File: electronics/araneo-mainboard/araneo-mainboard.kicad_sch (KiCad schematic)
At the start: 57 parts, among them J1 GPIO, J2 OLED, SW1 SW, U1 IMU, U2 L78M05CDT, U3 BD9C601EFJ, U4 POWER, U5 PAM8403D

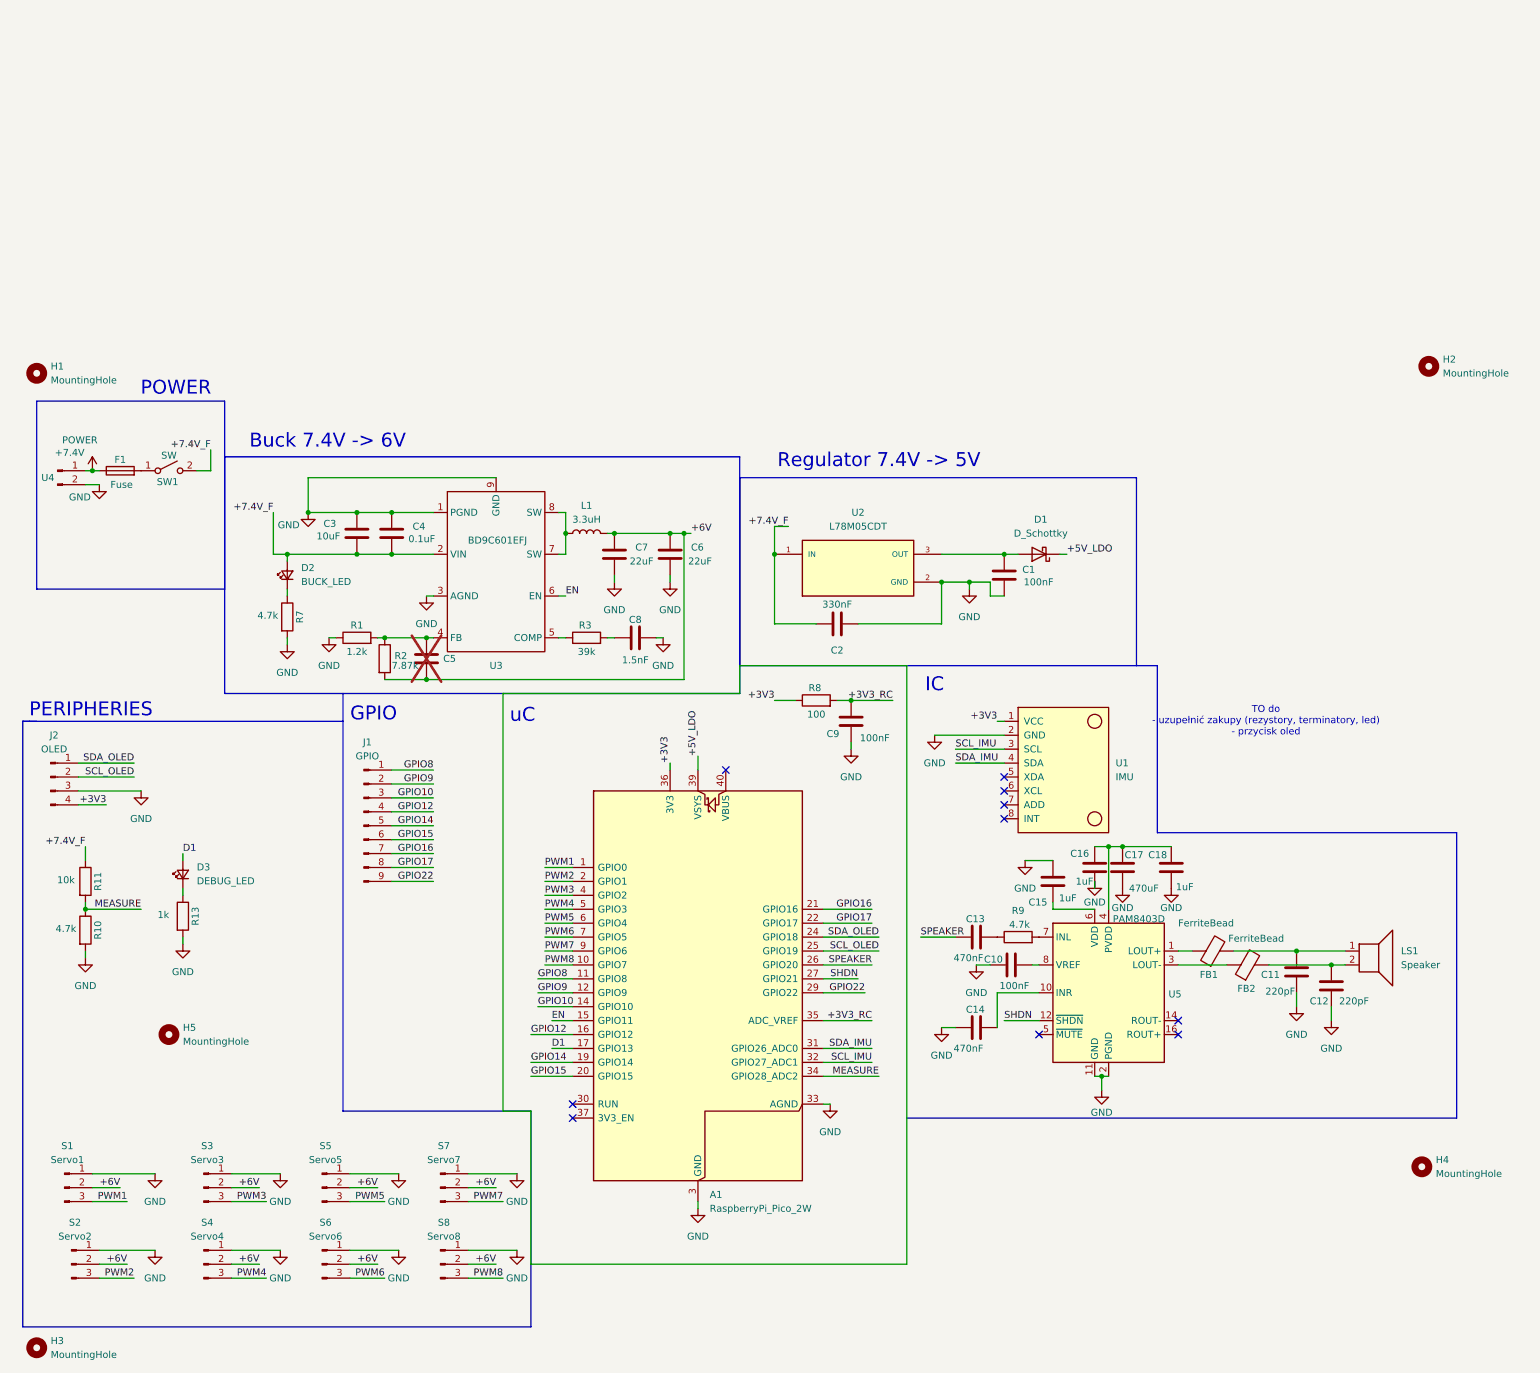
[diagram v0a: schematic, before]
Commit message: electronics: add button
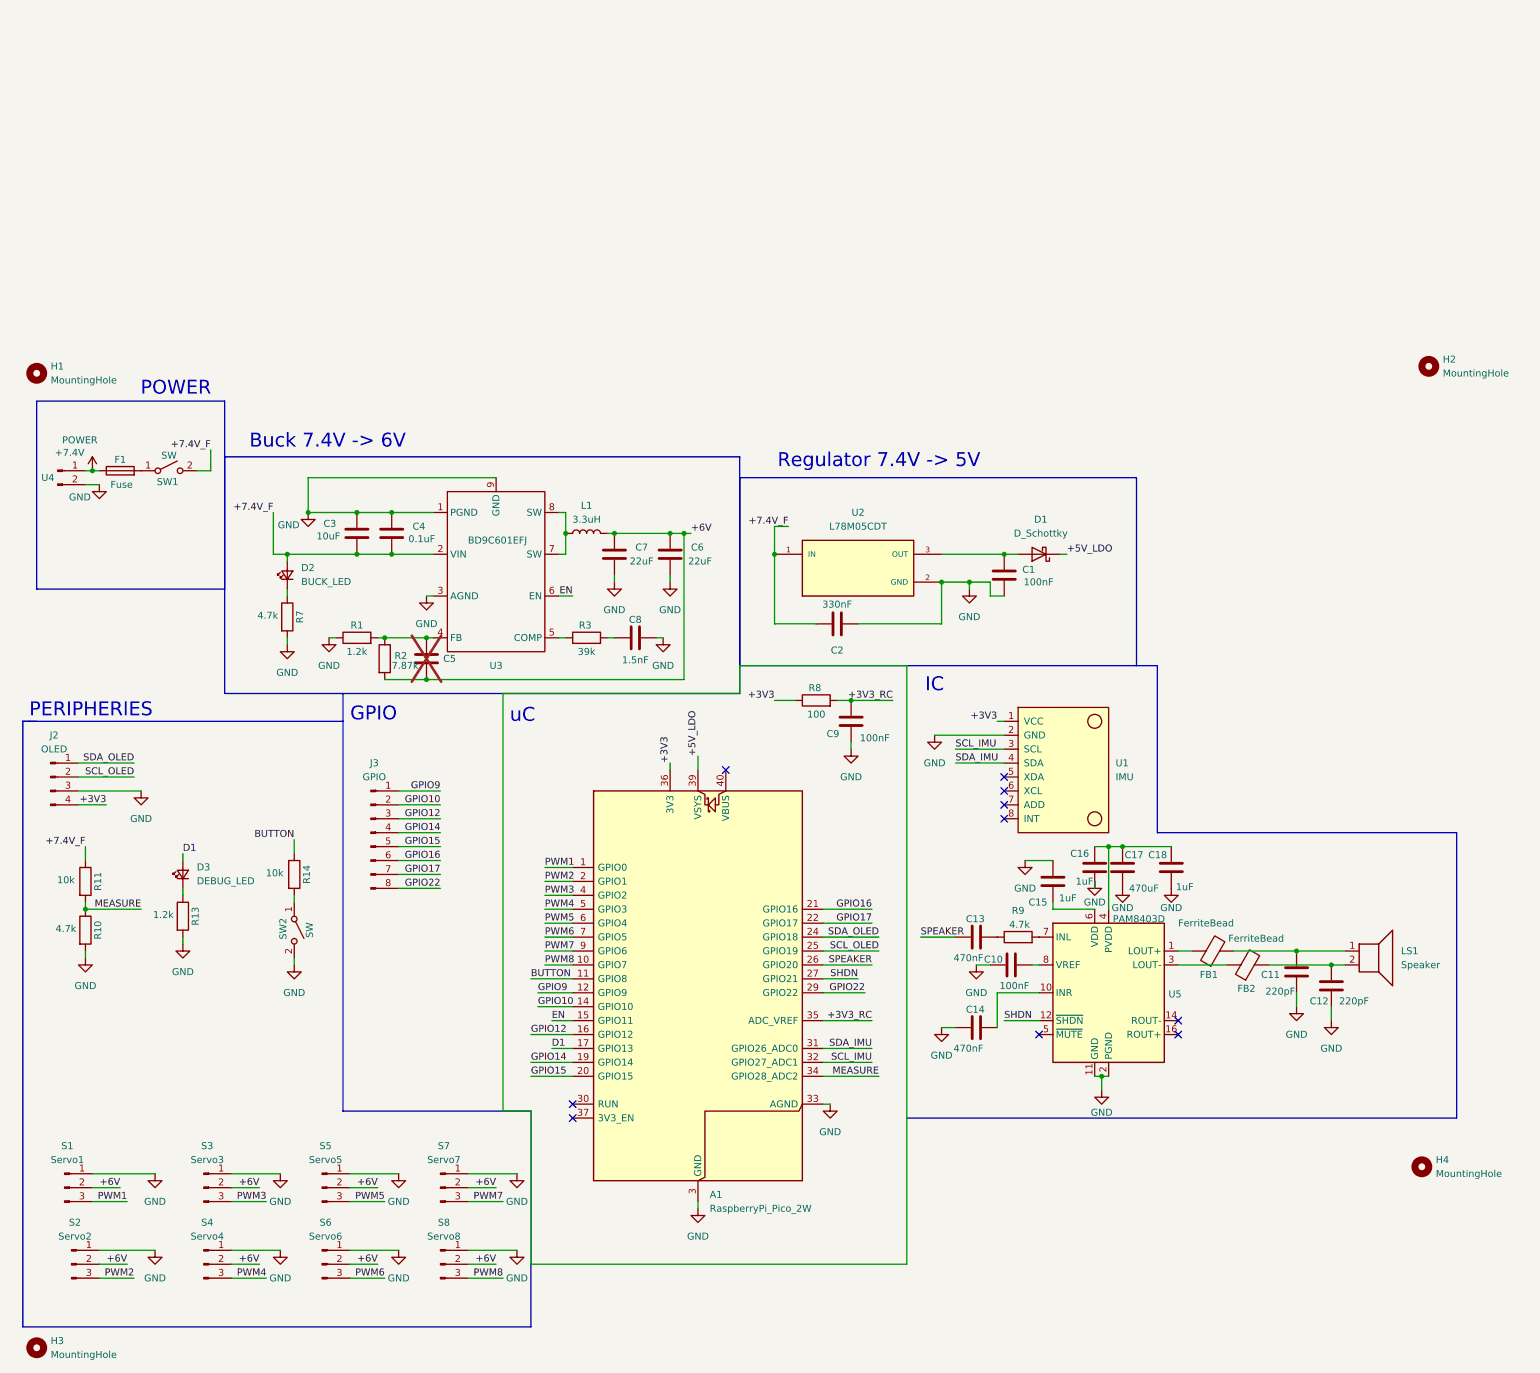
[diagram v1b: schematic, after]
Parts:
- removed H5: MountingHole, MountingHole:MountingHole_2.1mm, symbol Mechanical:MountingHole
- removed J1: GPIO, Connector_PinHeader_2.54mm:PinHeader_1x09_P2.54mm_Vertical, symbol Connector:Conn_01x09_Pin
- added J3: GPIO, Connector_PinHeader_2.54mm:PinHeader_1x08_P2.54mm_Vertical, symbol Connector:Conn_01x08_Pin
- added R14: 10k, Resistor_SMD:R_0603_1608Metric_Pad0.98x0.95mm_HandSolder, symbol Device:R
- added SW2: SW, PCM_SparkFun-Connector:ScrewTerminal_1x02_P3.5mm_Blue, symbol Switch:SW_SPST
- R13: value 1k -> 1.2k
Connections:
- net GND: now also SW2.2 (B)
- net GPIO10: now also J3.2 (Pin_2)
- net GPIO12: now also J3.3 (Pin_3)
- net GPIO14: now also J3.4 (Pin_4)
- net GPIO15: now also J3.5 (Pin_5)
- net GPIO16: now also J3.6 (Pin_6)
- net GPIO17: now also J3.7 (Pin_7)
- net GPIO22: now also J3.8 (Pin_8)
- net GPIO9: now also J3.1 (Pin_1)
- net GPIO8 renamed BUTTON
- net BUTTON: now also R14.1
- new net: R14.2, SW2.1 (A)
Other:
- note removed: "TO do - uzupełnić zakupy (rezystory, terminatory, led) - przycisk oled"

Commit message: electronics: add capacitor filters and Schottky diode
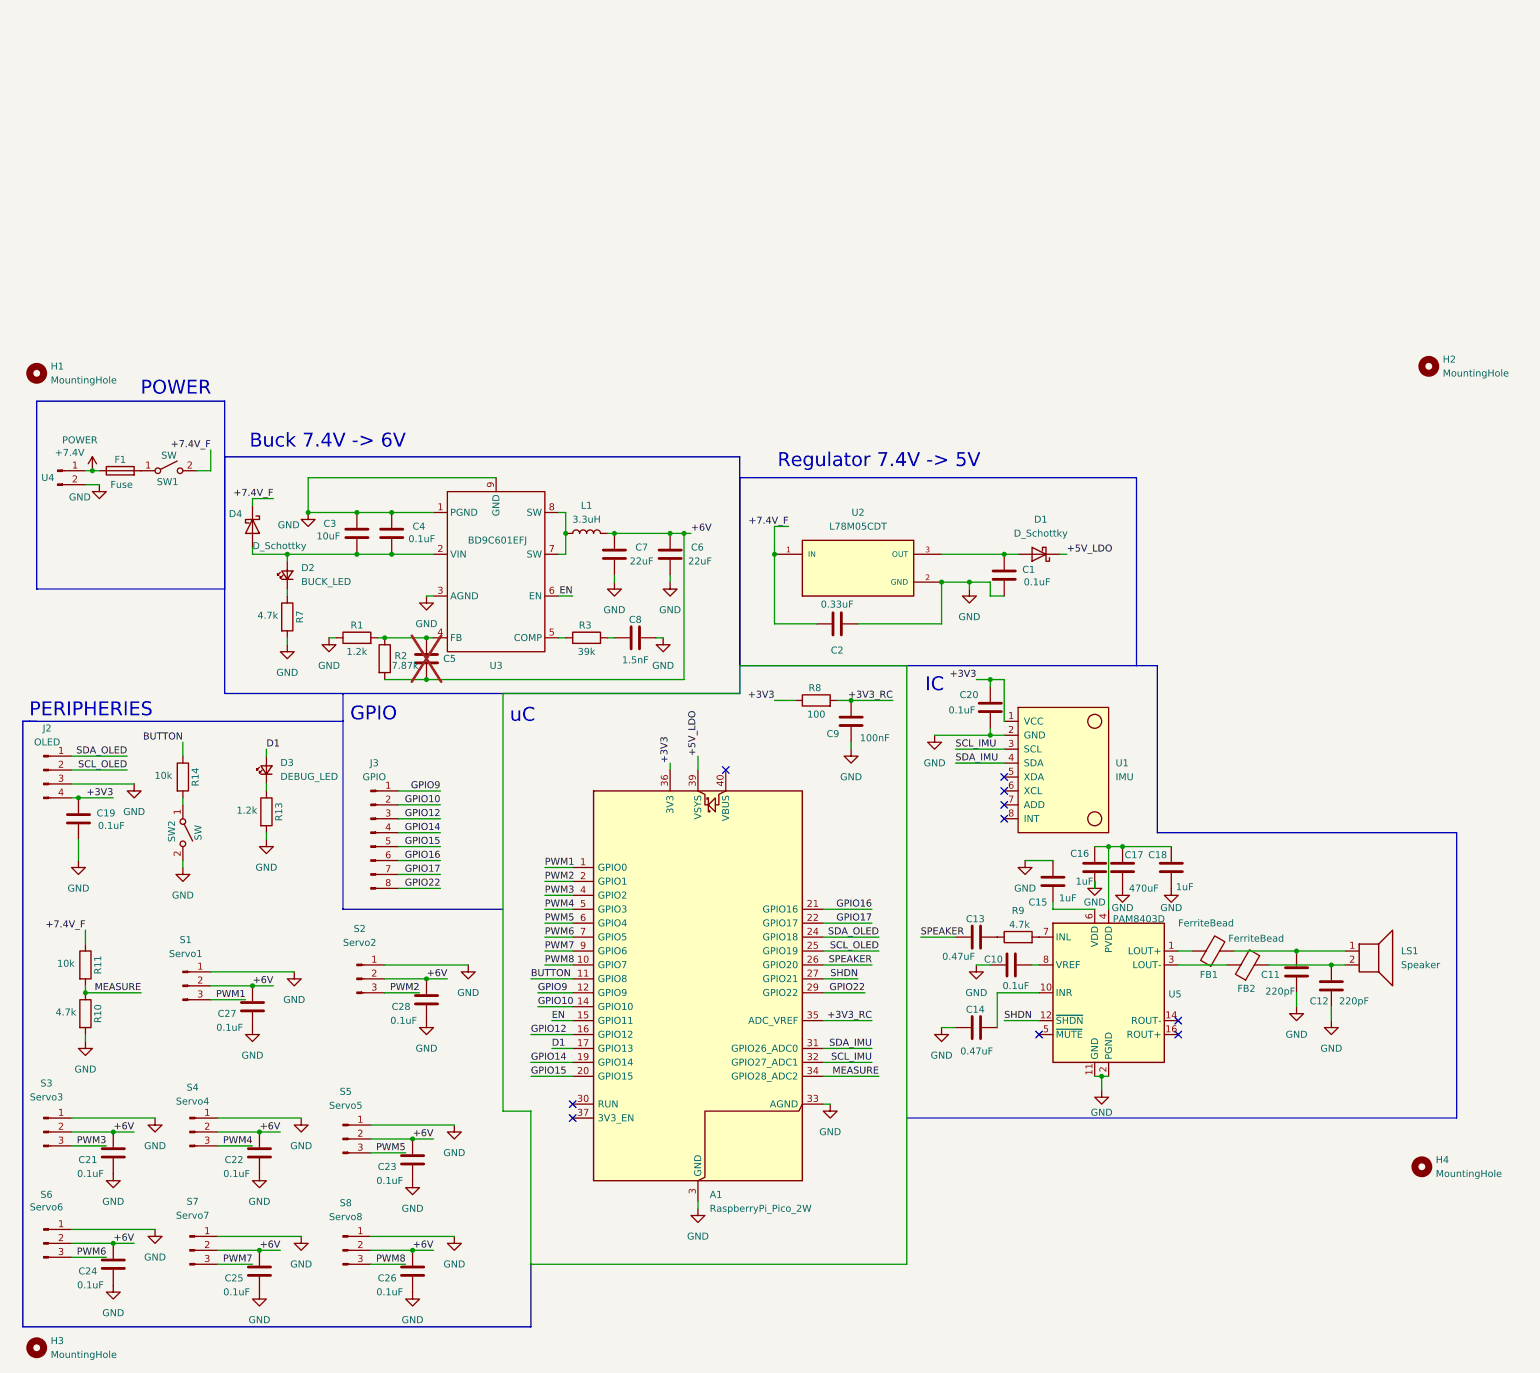
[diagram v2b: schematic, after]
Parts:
- removed S3: Servo3, Connector_PinHeader_2.54mm:PinHeader_1x03_P2.54mm_Vertical, symbol Connector:Conn_01x03_Pin
- added C19, C20, C21, C22, C23, C24, C25, C26, C27, C28: 0.1uF, Capacitor_SMD:C_0603_1608Metric_Pad1.08x0.95mm_HandSolder, symbol Device:C
- added D4: D_Schottky, Diode_THT:D_DO-41_SOD81_P10.16mm_Horizontal, symbol Device:D_Schottky
- added S1: Servo1, Connector_PinHeader_2.54mm:PinHeader_1x03_P2.54mm_Vertical, symbol Connector:Conn_01x03_Pin
- C1, C10: value 100nF -> 0.1uF
- C13, C14: value 470nF -> 0.47uF
- C2: value 330nF -> 0.33uF
- S3: renamed from S1; value Servo1 -> Servo3
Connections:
- net +3V3: now also C19.1, C20.1
- net +6V: now also C21.1, C22.1, C23.1, C24.1, C25.1, C26.1, C27.1, C28.1, S1.2 (Pin_2)
- net +7.4V_F: now also D4.1 (K); no longer C3.2, C4.2, D2.2 (A), U3.2 (VIN)
- net GND: now also C19.2, C20.2, C21.2, C22.2, C23.2, C24.2, C25.2, C26.2, C27.2, C28.2, S1.1 (Pin_1)
- net PWM1: now also S1.3 (Pin_3); no longer S3.3 (Pin_3)
- net PWM3: now also S3.3 (Pin_3)
- new net: C3.2, C4.2, D2.2 (A), D4.2 (A), U3.2 (VIN)
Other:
- moved on the sheet: D3, J2, R10, R11, R13, R14, S3, SW2
